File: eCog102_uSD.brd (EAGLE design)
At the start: 48 x 28 mm, 1 part

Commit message: V1.1
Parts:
- added R1, R2, R3: 47K, GadgetFactory_6.0:0805
- added SD1: MICROSD, adafruit:MICROSD
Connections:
- new net SD_!CS: ECOG.SPI-CS, R3.1, SD1.2
- new net SD_CD: SD1.CD1
- new net SD_MISO: ECOG.SPI-MISO, R1.1, SD1.7
- new net SD_MOSI: ECOG.SPI-MOSI, R2.1, SD1.3
- new net SD_SCK: ECOG.SPI-SCK, SD1.5
- net 3V3: now also R1.2, R2.2, R3.2, SD1.4
- net GND: now also SD1.6, SD1.MT1, SD1.MT2
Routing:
- net SD_SCK: track 0.00 -> 59.4 mm
- net SD_MOSI: track 0.00 -> 57.3 mm, vias 0 -> 2
- net SD_!CS: track 0.00 -> 57.0 mm, vias 0 -> 2
- net SD_MISO: track 0.00 -> 42.5 mm
- net 3V3: track 3.55 -> 20.1 mm, vias 1 -> 3
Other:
- board text added: "ecog102 v1.0"
- board text added: "ecog102.GadgetFactory.net"
- board text added: "uSD Card"
- board text removed: "5V"
- board text removed: "I2C-SCL"
- board text removed: "I2C-SDA"
- board text removed: "P5<>"
- board text removed: "Project Name"
- board text removed: "RESET"
- board text removed: "ecog100 v1.0"
- board text removed: "ecog100.GadgetFactory.net"

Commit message: Latest updated to V1.4
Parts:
- added U$1: (no value), GadgetFactory:GADGETBOX_TEXT
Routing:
- net 3V3: track 20.1 -> 33.5 mm
- net SD_SCK: track 59.4 -> 57.0 mm
- net SD_MOSI: track 57.3 -> 55.7 mm
- net SD_MISO: track 42.5 -> 40.9 mm
- net SD_!CS: track 57.0 -> 55.3 mm
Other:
- outline, holes or cut-outs redrawn
- board text added: "SPI-MISO>"
- board text added: "ecog102 v1.1"
- board text removed: "SPI-MOSI>"
- board text removed: "ecog102 v1.0"

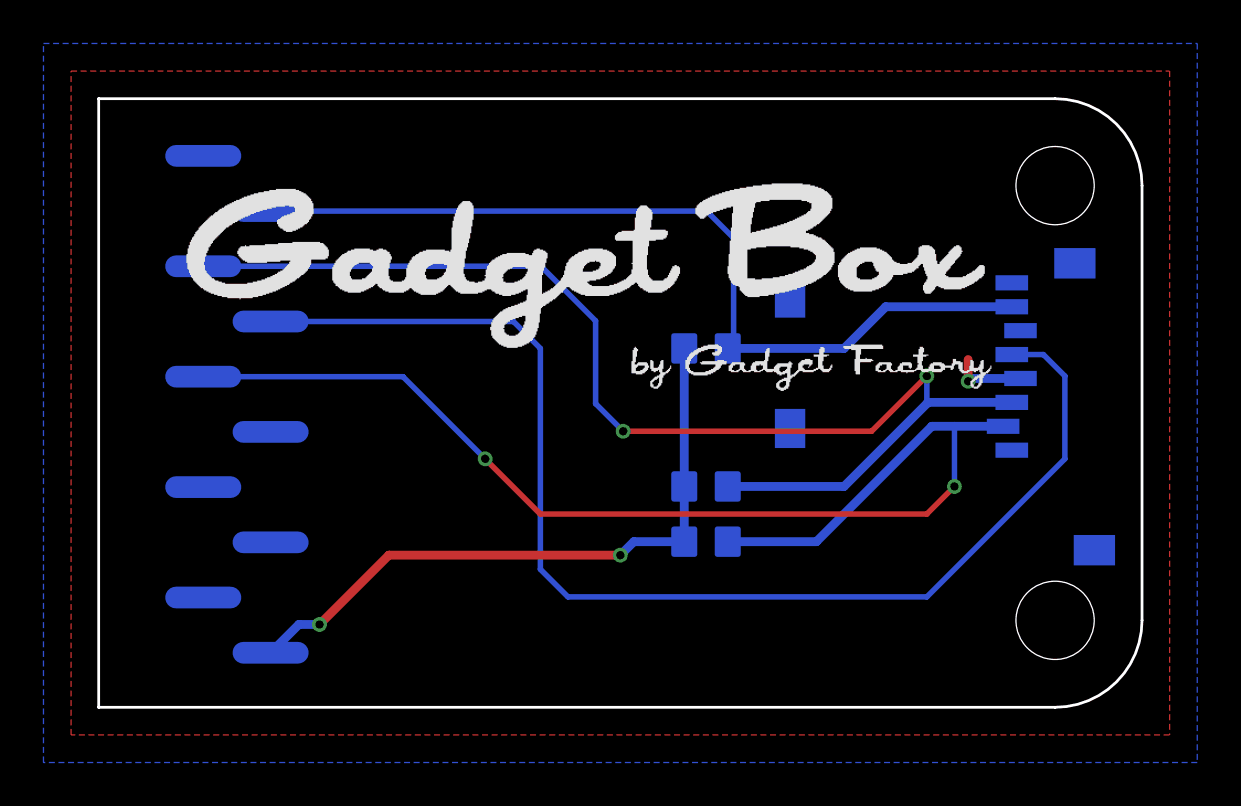
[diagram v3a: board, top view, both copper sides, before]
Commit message: Added Box text to silkscreen
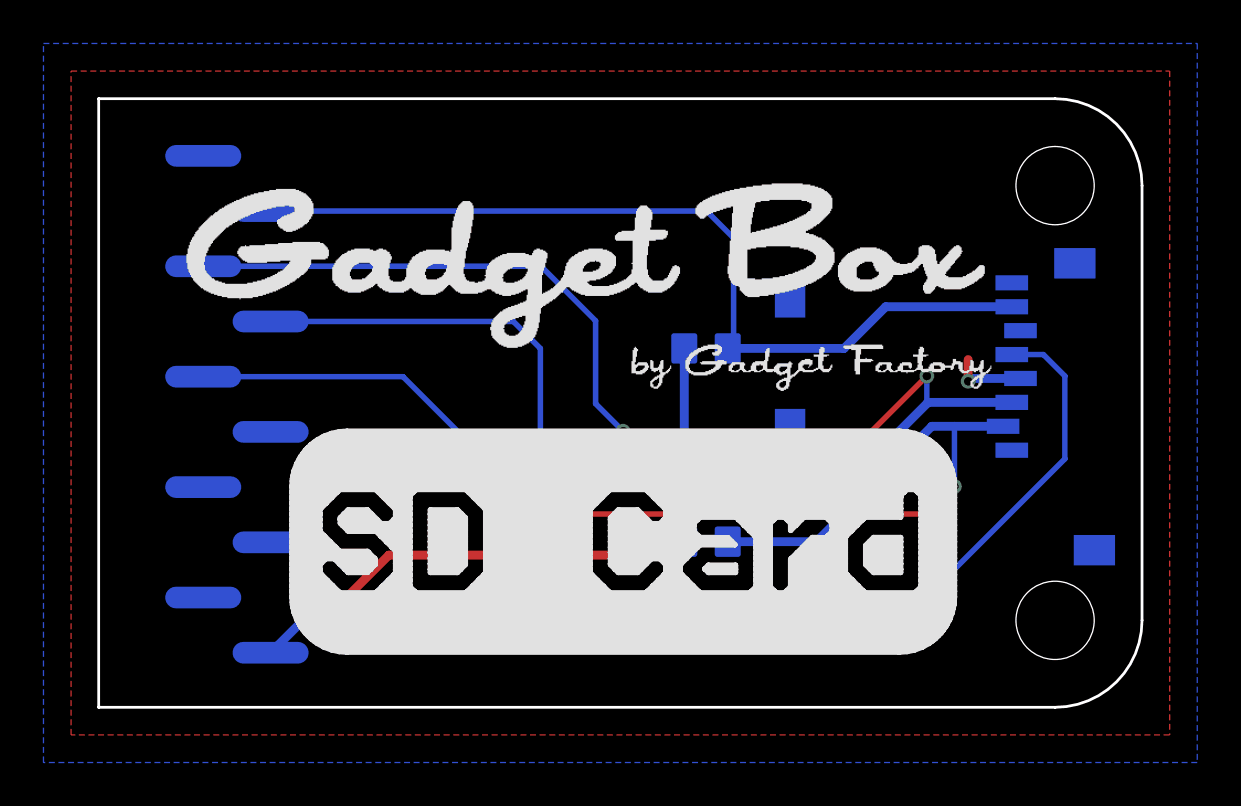
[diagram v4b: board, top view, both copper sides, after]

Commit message: Update all of the Fonts and graphics
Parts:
- added U$2: (no value), ohw-logo:OSHW_FILLX200_NOTEXT
- moved U$1 1.09 mm to (22.5, 19.3)

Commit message: All the 2.0 updates
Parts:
- moved U$1 1.76 mm to (24.0, 18.4)
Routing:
- net 3V3: track 33.5 -> 21.2 mm
- net SD_MISO: track 40.9 -> 52.3 mm
- net SD_MOSI: track 55.7 -> 46.8 mm
- net SD_SCK: track 57.0 -> 48.5 mm
- net SD_!CS: track 55.3 -> 48.7 mm
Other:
- board size 48 x 28 mm -> 47.5 x 28 mm
- board text added: "SPI-CS"
- board text added: "SPI-MISO"
- board text added: "SPI-MOSI"
- board text added: "SPI-SCK"
- board text added: "ecog102 v2.0"
- board text removed: "SPI-CS>"
- board text removed: "SPI-MISO>"
- board text removed: "SPI-MOSI<"
- board text removed: "SPI-SCK>"
- board text removed: "ecog102 v1.1"
